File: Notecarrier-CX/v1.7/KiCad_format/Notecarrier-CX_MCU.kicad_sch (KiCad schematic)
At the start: 33 parts, among them J5 Header 1.27mm 2X7, U5 STM32L433CCT6, U6 NX3L2467GU,115, Y1 ABS07-32.768KHZ-6-T

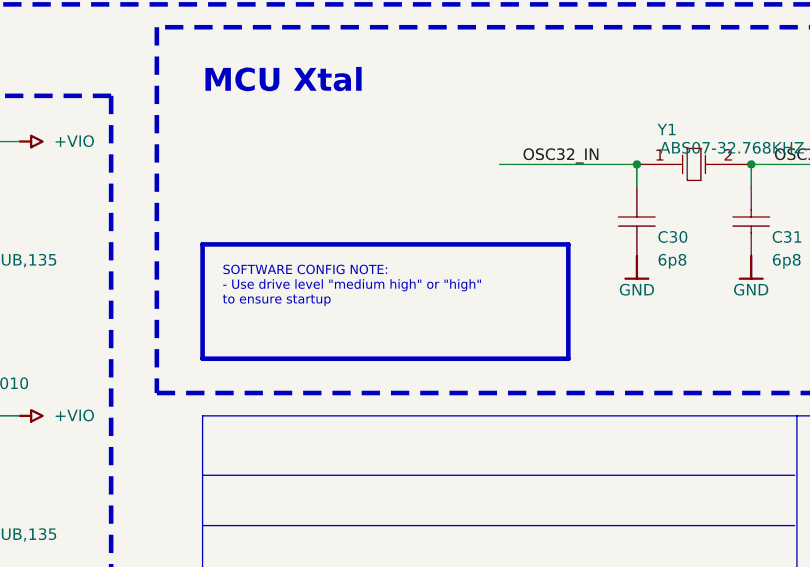
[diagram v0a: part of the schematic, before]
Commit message: Ports: convert design-note text_boxes to plain text so kicanvas can render them
kicanvas parses text_box but never paints it - true of the current upstream
build too, which is byte-identical to the one vendored here. On the published
datasheet pages that left the design notes (charger limits, regulator specs,
population notes) as empty frames, and on Cygnet, whose note frames ARE the
text_boxes, the notes were entirely invisible. KiCad renders plain text and
rectangles identically to what it drew before, and kicanvas renders both, so
the 28 text_boxes across 12 sheets on 6 boards become plain text items - plus a
synthesized rectangle carrying the exact stroke and fill for the 5 Cygnet notes
whose box itself is visible (yellow-filled with a border).

Two things made this more than a mechanical swap:

- text_box soft-wraps and plain text does not. A first attempt left two notes
  overflowing their frames and colliding with a neighbouring note. The wrap is
  now frozen at exactly the line breaks KiCad itself used: each sheet's
  before-conversion PDF carries a hidden searchable text layer, and the
  converter reads the wrapped lines out of the note's own rectangle, guarded by
  a word-for-word equality check against the source text. That guard earned its
  keep twice, catching part-number labels that physically overlap two of the
  note boxes.

- kicanvas draws default-colored text in its theme color, which is white - and
  two Cygnet notes sit on yellow fills. Those five framed notes now carry an
  explicit (0,0,193) font color, sampled from KiCad's own plot of the same
  notes, so KiCad's output is unchanged and kicanvas is readable.

Verified per board: netlists byte-equal before and after; KiCad PDF renders
differ only by sub-millimetre line pitch (0.05-0.7% of sampled pixels, every
note inside its frame - checked visually on the worst sheets); kicanvas renders
all 12 sheets with the notes now visible; committed screenshots regenerated,
all six boards PASS.

Co-Aut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
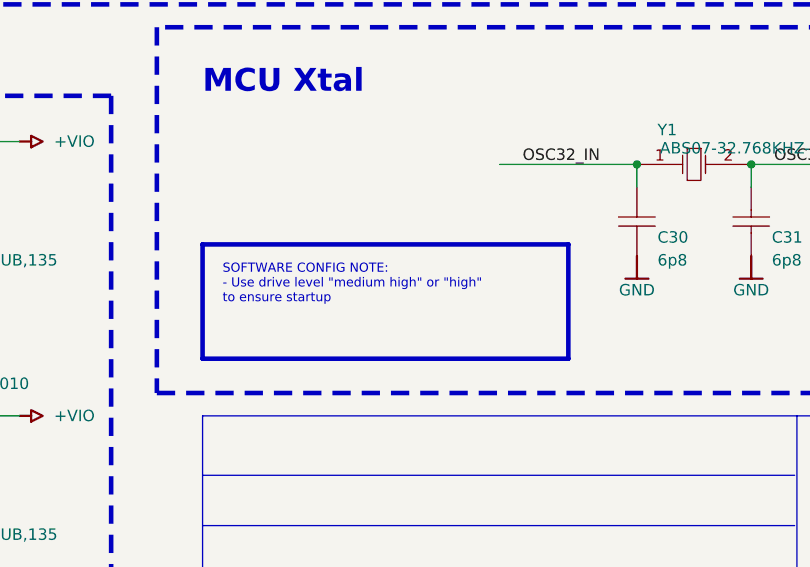
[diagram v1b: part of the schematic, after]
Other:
- note added: "SOFTWARE CONFIG NOTE: - Use drive level "medium high" or "high" to ensure startup"
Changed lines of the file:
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@@
 		)
 	)
-	(text_box "SOFTWARE CONFIG NOTE: \n- Use drive level \"medium high\" or \"high\" to ensure startup"
+	(text "SOFTWARE CONFIG NOTE:\n- Use drive level \"medium high\" or \"high\"\nto ensure startup"
 		(exclude_from_sim no)
-		(at 231.14 159.2072 0)
-		(size -36.83 10.16)
-		(margins 0.9525 0.9525 0.9525 0.9525)
-		(stroke
-			(width -0.0001)
-			(type default)
-			(color 0 0 0 1)
-		)
-		(fill
-			(type none)
-		)
+		(at 195.262 160.16 0)
 		(effects
 			(font
